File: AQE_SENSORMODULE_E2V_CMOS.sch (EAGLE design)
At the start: 33 parts, among them J1 440055-4, J2 AVR_SPI_PRG_6NS, U1 V_REG_LDOSMD, U2 V_REG_LDOSMD

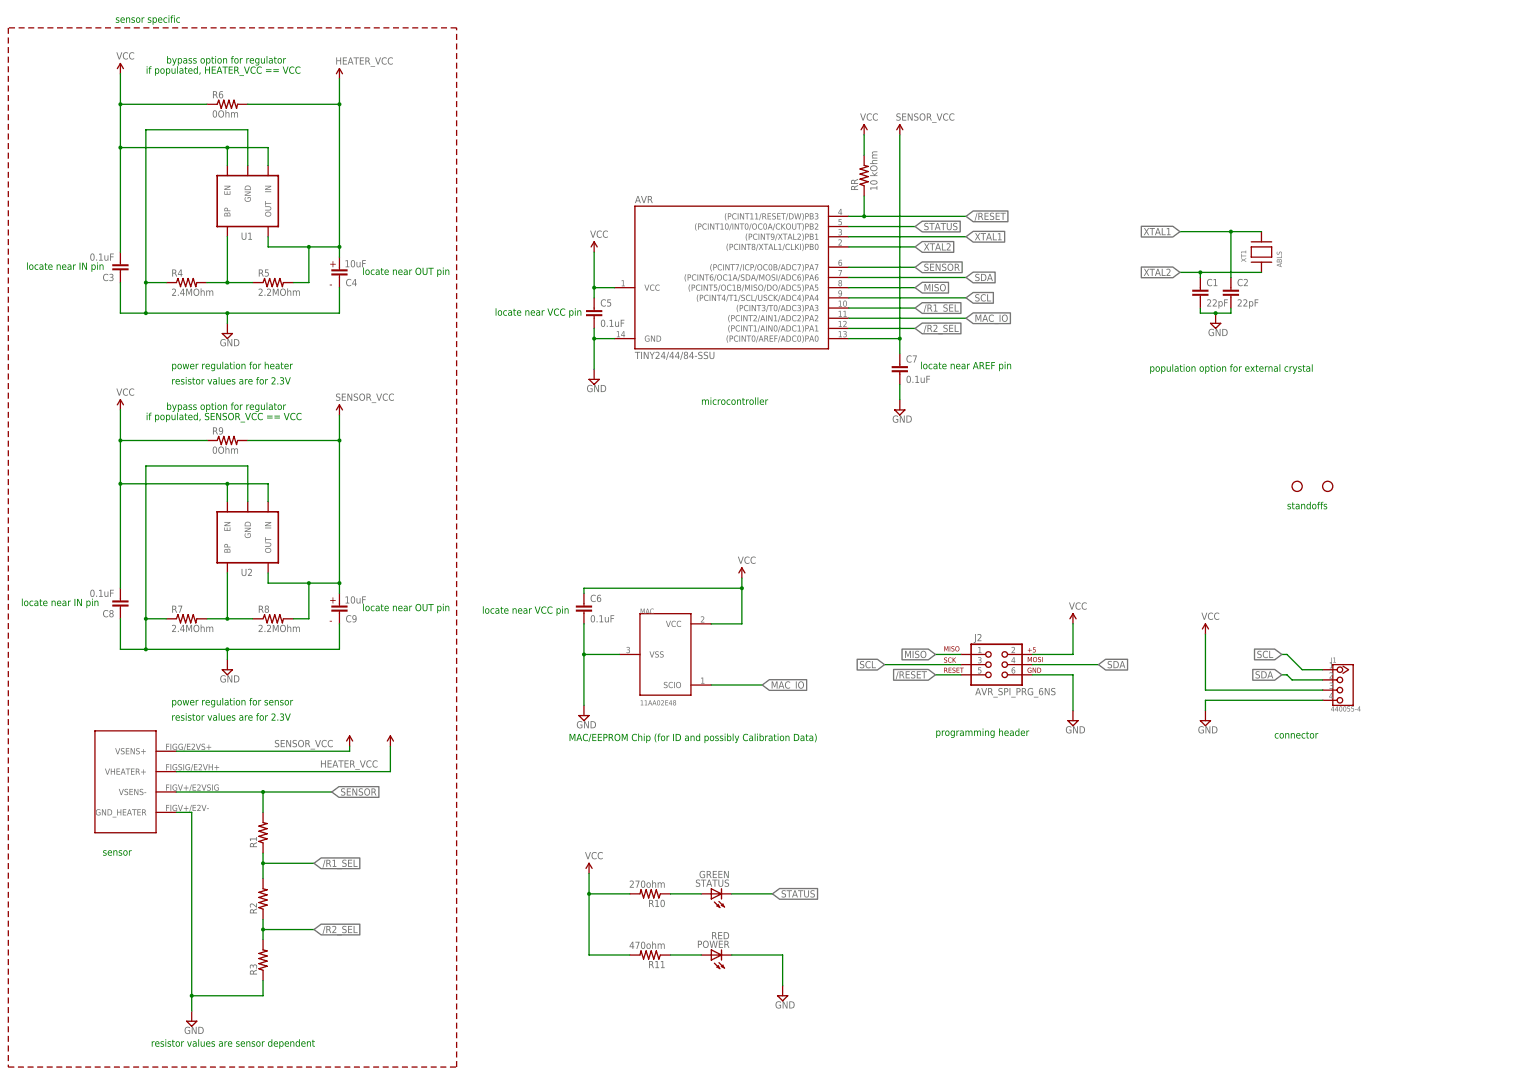
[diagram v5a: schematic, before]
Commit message: making progress on updates to incorporate heater feedback control
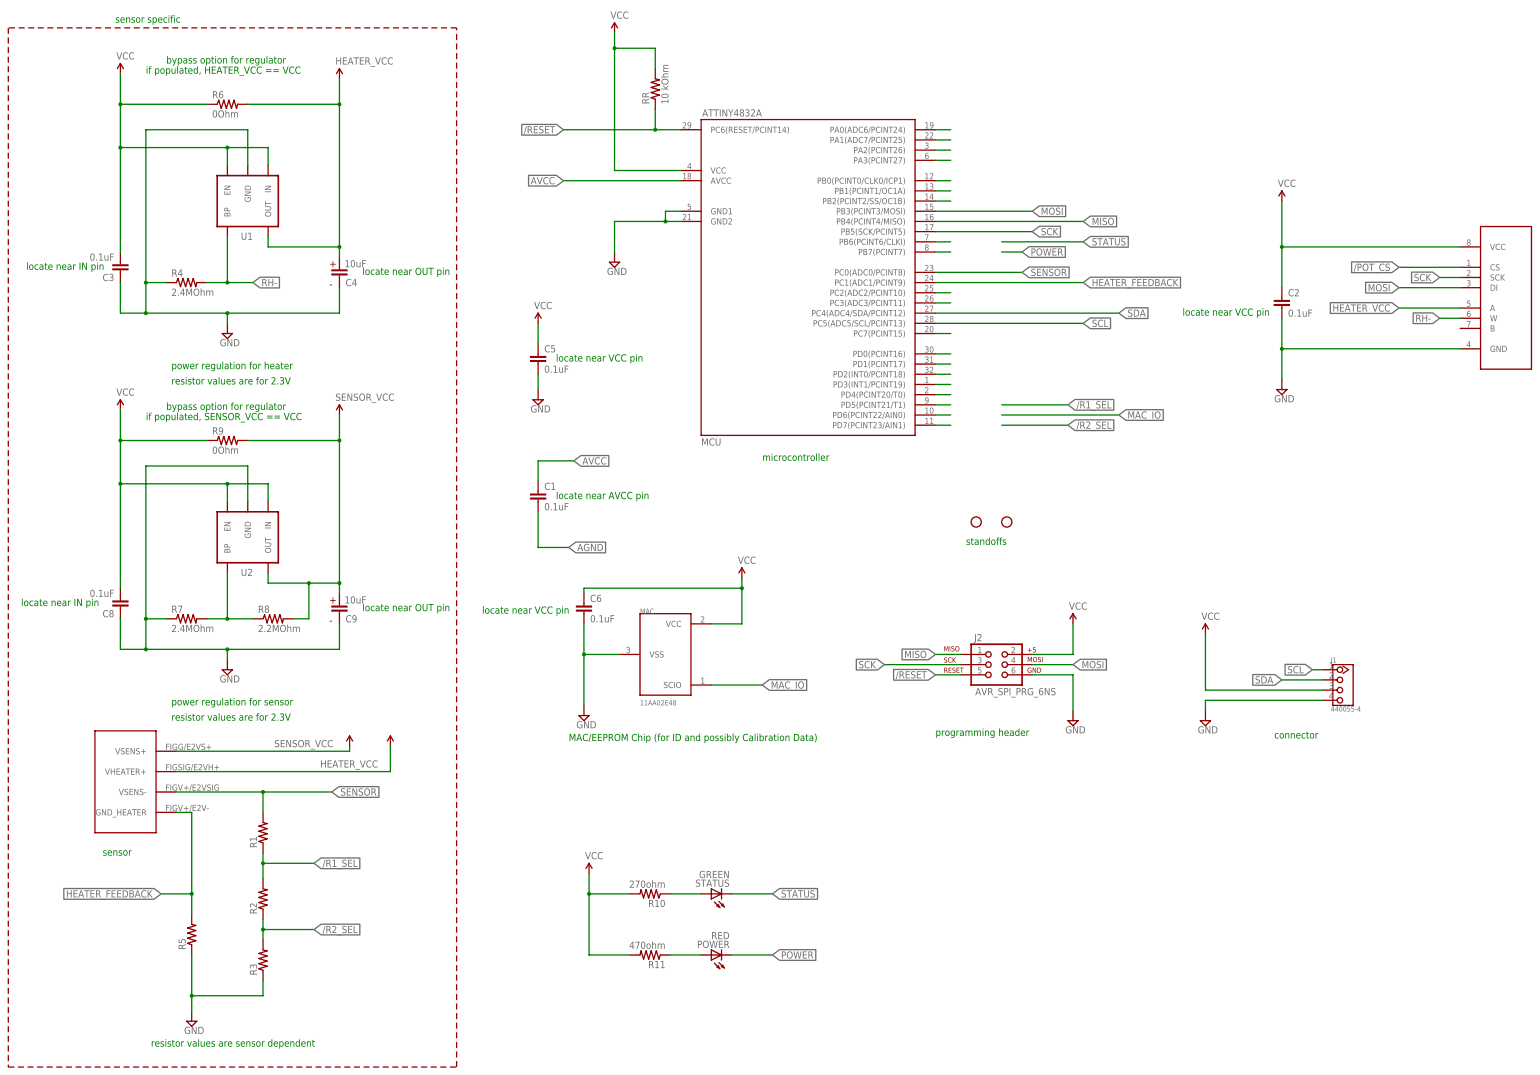
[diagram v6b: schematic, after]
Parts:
- removed AVR: TINY24/44/84-SSU, avr-7:TINY24/44/84-SSU
- removed C7: 0.1uF, SparkFun:CAP0603-CAP
- removed XT1: ABLS, wicked-device:ABLS
- added MCU: ATTINY4832A, axeio-SparkFun:ATTINY4832A
- added U3: MCP41XXX, SparkFun-AnalogIC:MCP41XXX
- C1, C2: value 22pF -> 0.1uF
- R5: value 2.2MOhm -> (none)
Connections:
- removed net N$1: R4.2, R5.1, U1.BP
- removed net XTAL1: AVR.(PCINT9/XTAL2)PB1, C2.1, XT1.P$2
- removed net XTAL2: AVR.(PCINT8/XTAL1/CLKI)PB0, C1.1, XT1.P$1
- new net /POT_CS: U3.CS
- new net AGND: C1.2
- new net AVCC: C1.1, MCU.AVCC
- new net HEATER_FEEDBACK: MCU.PC1(ADC1/PCINT9), R5.2, U$4.GND_HEATER
- new net MOSI: J2.4, MCU.PB3(PCINT3/MOSI), U3.DI
- new net N$10: MCU.PB1(PCINT1/OC1A)
- new net N$11: MCU.PB2(PCINT2/SS/OC1B)
- new net N$15: MCU.PB6(PCINT6/CLKI)
- new net N$16: MCU.PB7(PCINT7)
- new net N$19: MCU.PC2(ADC2/PCINT10)
- new net N$20: MCU.PC3(ADC3/PCINT11)
- new net N$23: MCU.PC7(PCINT15)
- new net N$24: MCU.PD0(PCINT16)
- new net N$25: MCU.PD1(PCINT17)
- new net N$26: MCU.PD2(INT0/PCINT18)
- new net N$27: MCU.PD3(INT1/PCINT19)
- new net N$28: MCU.PD4(PCINT20/T0)
- new net N$29: MCU.PD5(PCINT21/T1)
- new net N$30: MCU.PD6(PCINT22/AIN0)
- new net N$31: MCU.PD7(PCINT23/AIN1)
- new net N$5: MCU.PA0(ADC6/PCINT24)
- new net N$6: MCU.PA1(ADC7/PCINT25)
- new net N$7: MCU.PA2(PCINT26)
- new net N$8: MCU.PA3(PCINT27)
- new net N$9: MCU.PB0(PCINT0/CLK0/ICP1)
- new net POWER: POWER.C
- new net RH-: R4.2, U1.BP, U3.W
- new net SCK: J2.3, MCU.PB5(SCK/PCINT5), U3.SCK
- net /R1_SEL: no longer AVR.(PCINT3/T0/ADC3)PA3
- net /R2_SEL: no longer AVR.(PCINT1/AIN0/ADC1)PA1
- net /RESET: now also MCU.PC6(RESET/PCINT14); no longer AVR.(PCINT11/RESET/DW)PB3
- net GND: now also MCU.GND1, MCU.GND2, R5.1, U3.GND; no longer AVR.GND, C1.2, C7.2, POWER.C, U$4.GND_HEATER
- net HEATER_VCC: now also U3.A; no longer R5.2
- net MAC_IO: no longer AVR.(PCINT2/AIN1/ADC2)PA2
- net MISO: now also MCU.PB4(PCINT4/MISO); no longer AVR.(PCINT5/OC1B/MISO/DO/ADC5)PA5
- net SCL: now also MCU.PC5(ADC5/SCL/PCINT13); no longer AVR.(PCINT4/T1/SCL/USCK/ADC4)PA4, J2.3
- net SDA: now also MCU.PC4(ADC4/SDA/PCINT12); no longer AVR.(PCINT6/OC1A/SDA/MOSI/ADC6)PA6, J2.4
- net SENSOR: now also MCU.PC0(ADC0/PCINT8); no longer AVR.(PCINT7/ICP/OC0B/ADC7)PA7
- net SENSOR_VCC: no longer AVR.(PCINT0/AREF/ADC0)PA0, C7.1
- net STATUS: no longer AVR.(PCINT10/INT0/OC0A/CKOUT)PB2
- net VCC: now also C2.1, MCU.VCC, U3.VCC; no longer AVR.VCC
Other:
- note added: "locate near AVCC pin"
- note removed: "locate near AREF pin"
- note removed: "population option for external crystal"
- moved on the sheet: C1, C2, C5, R5, RR

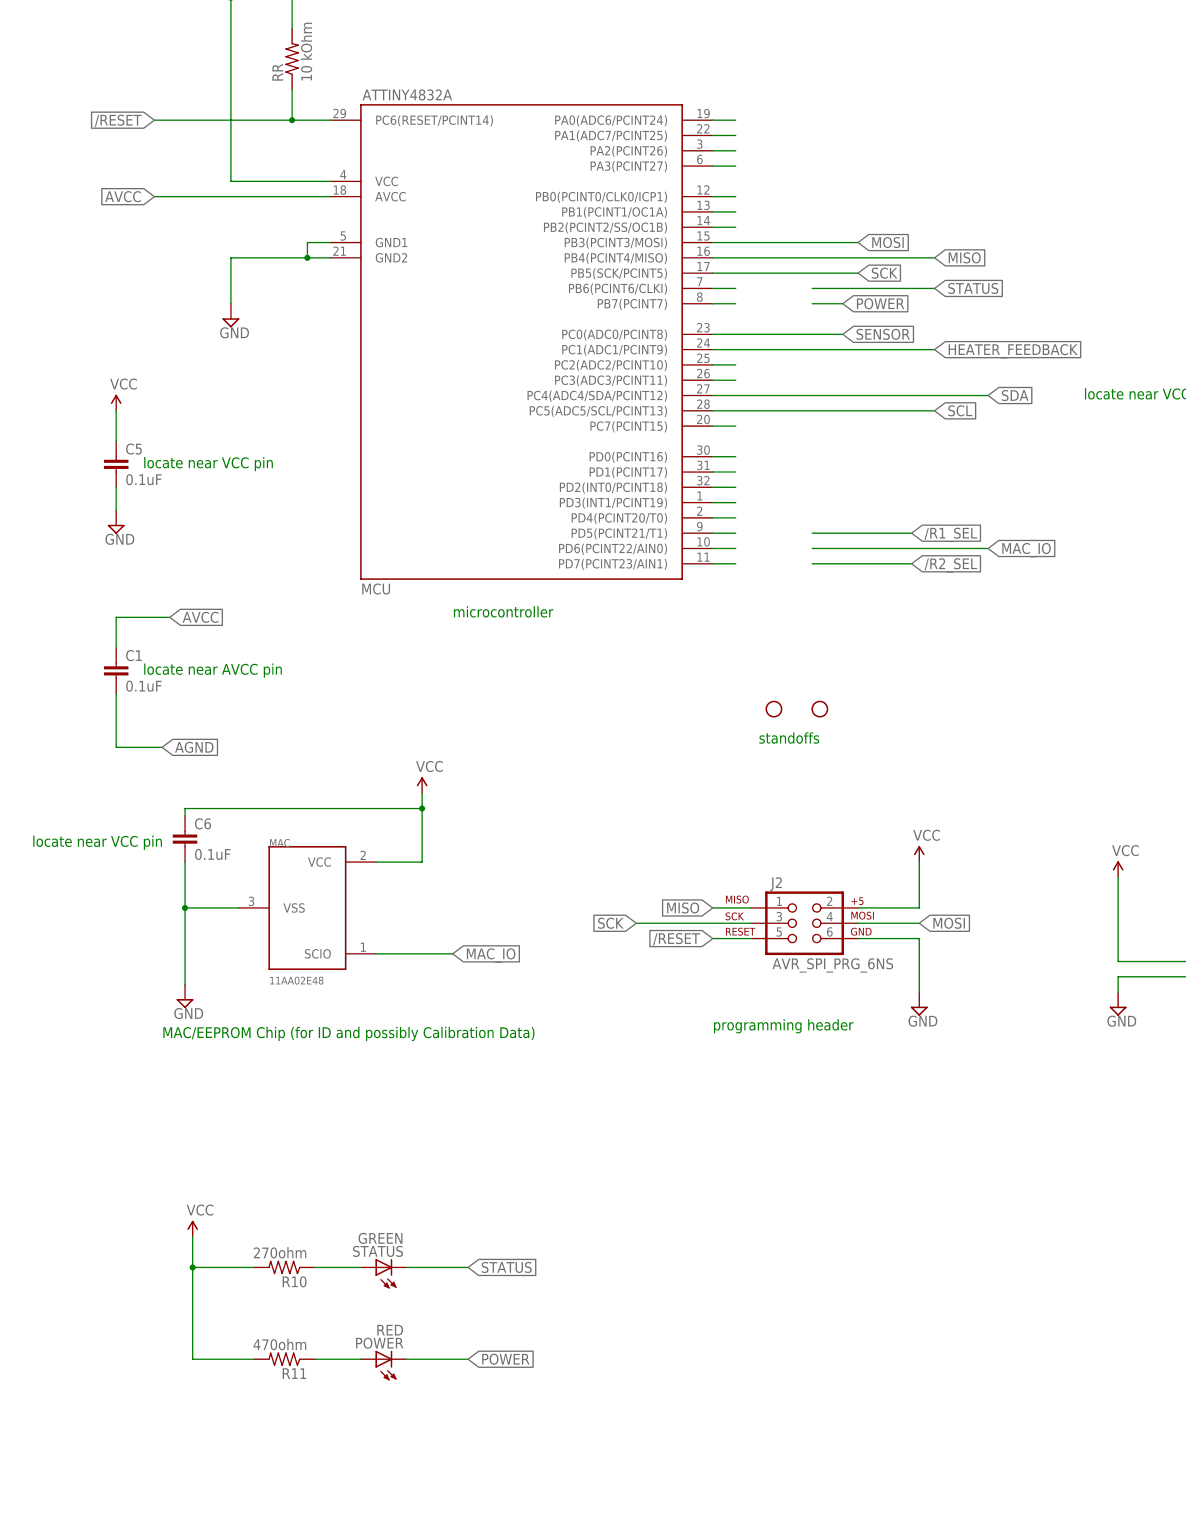
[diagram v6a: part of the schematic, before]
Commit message: routed additional signals, would like to separate analog ground plane
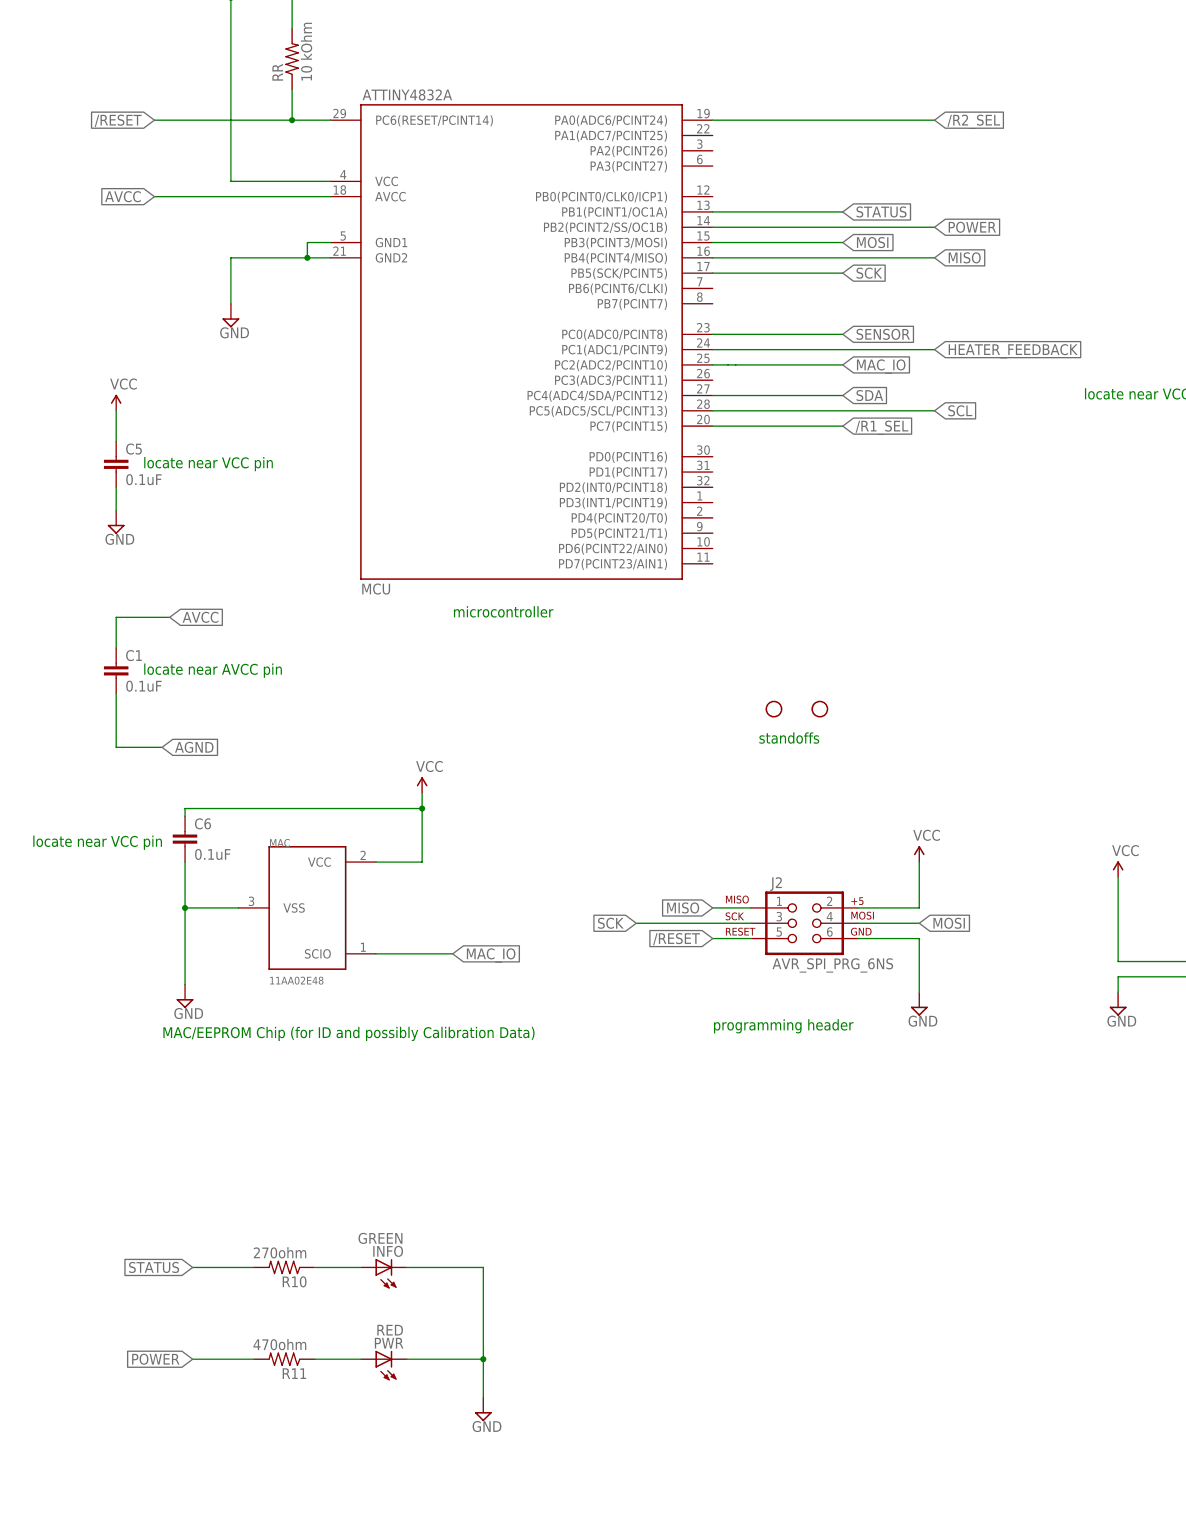
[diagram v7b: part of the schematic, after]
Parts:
- renumbered POWER to PWR, STATUS to INFO
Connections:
- removed net N$10: MCU.PB1(PCINT1/OC1A)
- removed net N$11: MCU.PB2(PCINT2/SS/OC1B)
- removed net N$15: MCU.PB6(PCINT6/CLKI)
- removed net N$16: MCU.PB7(PCINT7)
- removed net N$19: MCU.PC2(ADC2/PCINT10)
- removed net N$20: MCU.PC3(ADC3/PCINT11)
- removed net N$23: MCU.PC7(PCINT15)
- removed net N$24: MCU.PD0(PCINT16)
- removed net N$25: MCU.PD1(PCINT17)
- removed net N$26: MCU.PD2(INT0/PCINT18)
- removed net N$27: MCU.PD3(INT1/PCINT19)
- removed net N$28: MCU.PD4(PCINT20/T0)
- removed net N$29: MCU.PD5(PCINT21/T1)
- removed net N$30: MCU.PD6(PCINT22/AIN0)
- removed net N$31: MCU.PD7(PCINT23/AIN1)
- removed net N$5: MCU.PA0(ADC6/PCINT24)
- removed net N$6: MCU.PA1(ADC7/PCINT25)
- removed net N$7: MCU.PA2(PCINT26)
- removed net N$8: MCU.PA3(PCINT27)
- removed net N$9: MCU.PB0(PCINT0/CLK0/ICP1)
- net /R1_SEL: now also MCU.PC7(PCINT15)
- net /R2_SEL: now also MCU.PA0(ADC6/PCINT24)
- net GND: now also INFO.C, PWR.C
- net MAC_IO: now also MCU.PC2(ADC2/PCINT10)
- net POWER: now also MCU.PB2(PCINT2/SS/OC1B), R11.2; no longer PWR.C
- net STATUS: now also MCU.PB1(PCINT1/OC1A), R10.2; no longer INFO.C
- net VCC: no longer R10.2, R11.2

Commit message: incorporated changes for separating analog and digital gnd with a star topology. added possibility to shut off heater power, and added power filtering for analog vcc to mcu
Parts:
- added L1: FERRITE, nanodeRF_11:RCL_R-EU_R0805
- added U$2, U$3: PLANE_COUPLER, wicked-device:PLANE_COUPLER
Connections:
- new net HEATER_EN: MCU.PC3(ADC3/PCINT11), U1.EN
- new net RETURN_GND: J1.4, U$2.P$2, U$3.P$2
- net AGND: now also MCU.GND2, U$2.P$1
- net AVCC: now also L1.1
- net GND: now also U$3.P$1; no longer J1.4, MCU.GND2
- net VCC: now also L1.2; no longer U1.EN
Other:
- note added: "analog power filtering"
- note added: "digital potentiometer for heater feedback control"
- note added: "star topology for separating analog and digital GND"
- moved on the sheet: C1, J1
